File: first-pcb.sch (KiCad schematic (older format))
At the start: 91 parts, among them J1 OLED, SW1 SW_Push, U1 kbd_ProMicro

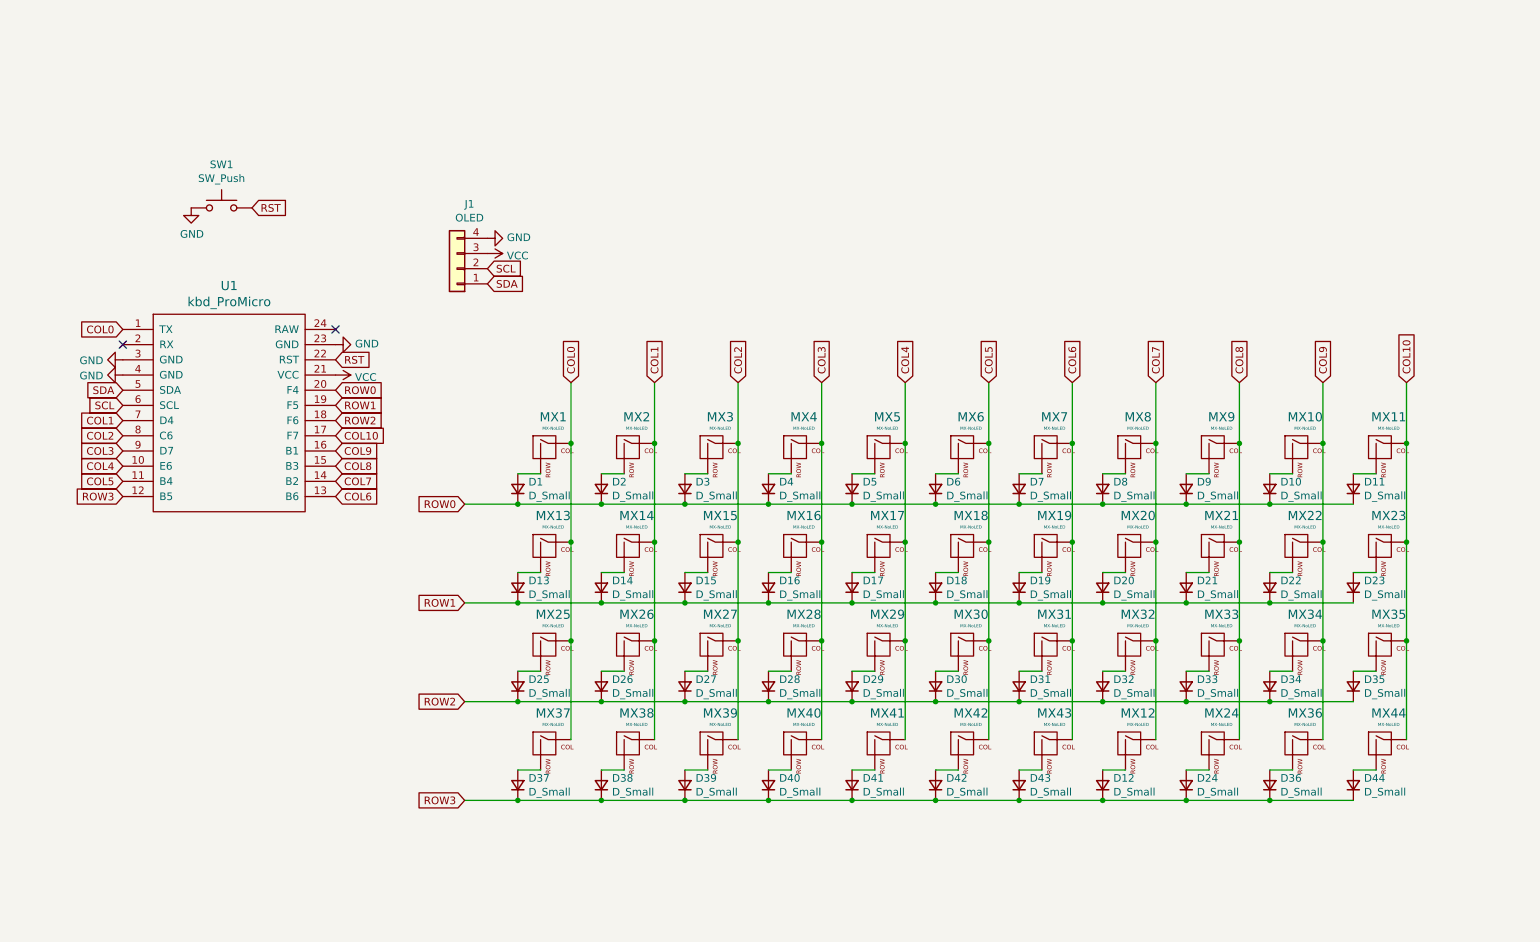
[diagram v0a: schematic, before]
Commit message: Version 0.1.1 (#2)
* New routing to use less pin

* Add LED on the schema

* Routing the LED

* Change the silks to display switch info

* add the plate dxf file

* Rename contour in bottom
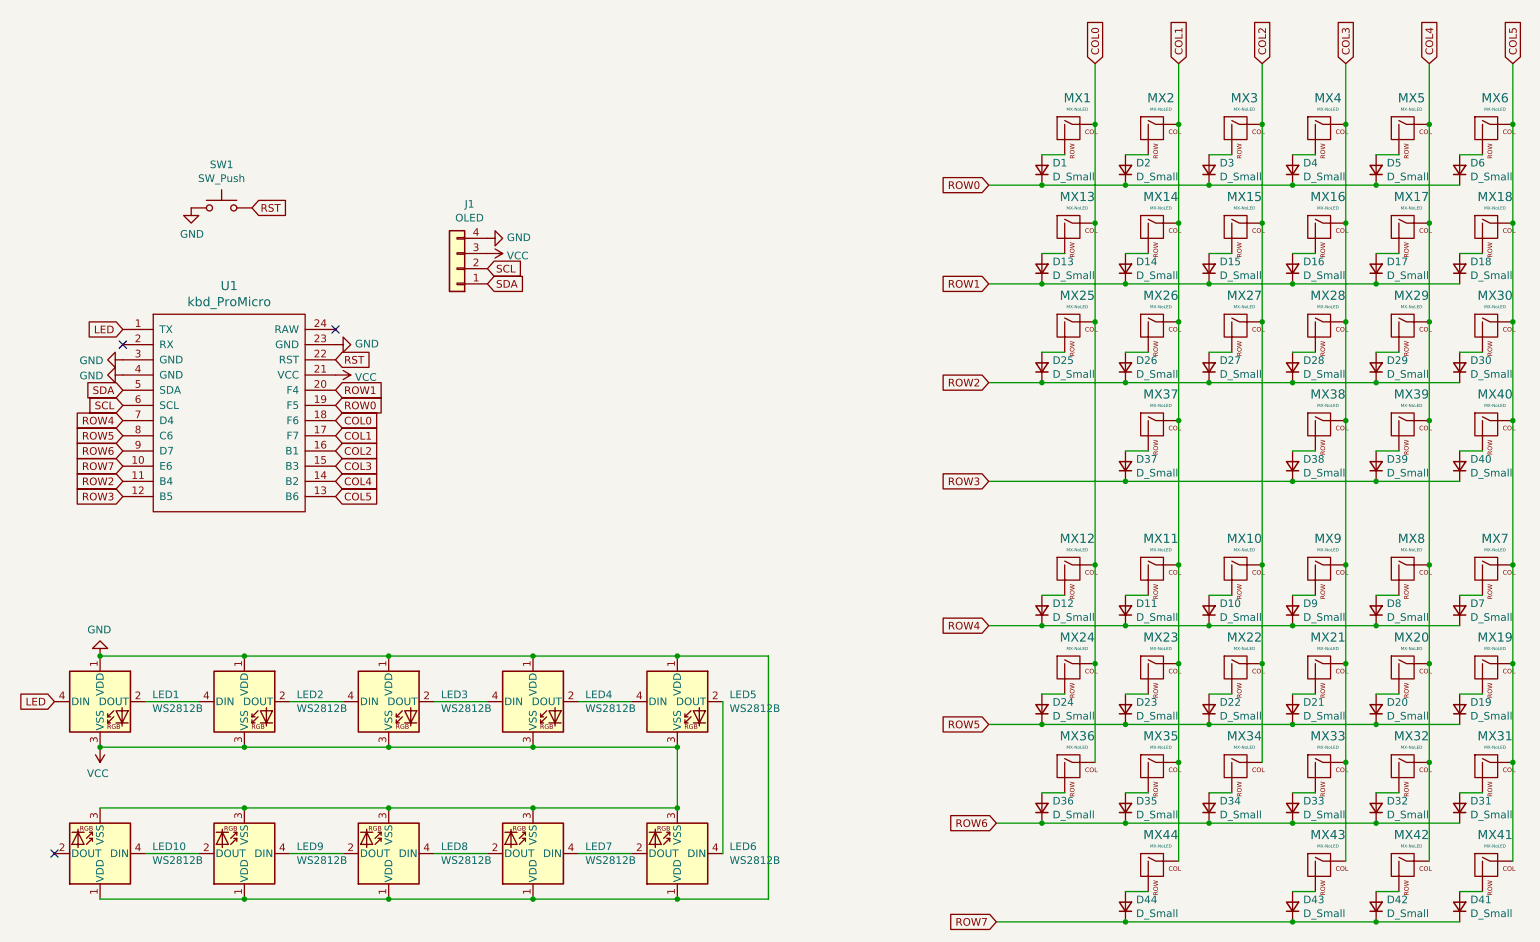
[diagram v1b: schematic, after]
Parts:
- added LED1, LED10, LED2, LED3, LED4, LED5, LED6, LED7, LED8, LED9: WS2812B, LED_SMD:LED_WS2812B_PLCC4_5.0x5.0mm_P3.2mm, symbol LED:WS2812B
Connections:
- net COL10 is gone; now on net COL1: MX11.1 (COL), MX23.1 (COL), MX35.1 (COL), MX44.1 (COL), U1.17 (F7)
- net COL0: now also MX12.1 (COL), MX24.1 (COL), MX36.1 (COL), U1.18 (F6); no longer MX37.1 (COL), U1.1 (TX)
- net COL1: now also MX37.1 (COL); no longer MX38.1 (COL), U1.7 (D4)
- net COL2: now also MX10.1 (COL), MX22.1 (COL), MX34.1 (COL), U1.16 (B1); no longer MX39.1 (COL), U1.8 (C6)
- net COL3: now also MX21.1 (COL), MX33.1 (COL), MX38.1 (COL), MX43.1 (COL), MX9.1 (COL), U1.15 (B3); no longer MX40.1 (COL), U1.9 (D7)
- net COL4: now also MX20.1 (COL), MX32.1 (COL), MX39.1 (COL), MX42.1 (COL), MX8.1 (COL), U1.14 (B2); no longer MX41.1 (COL), U1.10 (E6)
- net COL5: now also MX19.1 (COL), MX31.1 (COL), MX40.1 (COL), MX41.1 (COL), MX7.1 (COL), U1.13 (B6); no longer MX42.1 (COL), U1.11 (B4)
- net GND: now also LED1.1 (VDD), LED10.1 (VDD), LED2.1 (VDD), LED3.1 (VDD), LED4.1 (VDD), LED5.1 (VDD), LED6.1 (VDD), LED7.1 (VDD), LED8.1 (VDD), LED9.1 (VDD)
- net ROW0: now also U1.19 (F5); no longer D10.1 (K), D11.1 (K), D7.1 (K), D8.1 (K), D9.1 (K), U1.20 (F4)
- net ROW1: now also U1.20 (F4); no longer D19.1 (K), D20.1 (K), D21.1 (K), D22.1 (K), D23.1 (K), U1.19 (F5)
- net ROW2: now also U1.11 (B4); no longer D31.1 (K), D32.1 (K), D33.1 (K), D34.1 (K), D35.1 (K), U1.18 (F6)
- net ROW3: no longer D12.1 (K), D24.1 (K), D36.1 (K), D41.1 (K), D42.1 (K), D43.1 (K), D44.1 (K)
- net VCC: now also LED1.3 (VSS), LED10.3 (VSS), LED2.3 (VSS), LED3.3 (VSS), LED4.3 (VSS), LED5.3 (VSS), LED6.3 (VSS), LED7.3 (VSS), LED8.3 (VSS), LED9.3 (VSS)
- removed net COL6: MX19.1 (COL), MX31.1 (COL), MX43.1 (COL), MX7.1 (COL), U1.13 (B6)
- removed net COL7: MX12.1 (COL), MX20.1 (COL), MX32.1 (COL), MX8.1 (COL), U1.14 (B2)
- removed net COL8: MX21.1 (COL), MX24.1 (COL), MX33.1 (COL), MX9.1 (COL), U1.15 (B3)
- removed net COL9: MX10.1 (COL), MX22.1 (COL), MX34.1 (COL), MX36.1 (COL), U1.16 (B1)
- new net: LED1.2 (DOUT), LED2.4 (DIN)
- new net: LED2.2 (DOUT), LED3.4 (DIN)
- new net: LED3.2 (DOUT), LED4.4 (DIN)
- new net: LED4.2 (DOUT), LED5.4 (DIN)
- new net: LED5.2 (DOUT), LED6.4 (DIN)
- new net: LED10.4 (DIN), LED9.2 (DOUT)
- new net: LED8.2 (DOUT), LED9.4 (DIN)
- new net: LED7.2 (DOUT), LED8.4 (DIN)
- new net: LED6.2 (DOUT), LED7.4 (DIN)
- new net LED: LED1.4 (DIN), U1.1 (TX)
- new net ROW4: D10.1 (K), D11.1 (K), D12.1 (K), D7.1 (K), D8.1 (K), D9.1 (K), U1.7 (D4)
- new net ROW5: D19.1 (K), D20.1 (K), D21.1 (K), D22.1 (K), D23.1 (K), D24.1 (K), U1.8 (C6)
- new net ROW6: D31.1 (K), D32.1 (K), D33.1 (K), D34.1 (K), D35.1 (K), D36.1 (K), U1.9 (D7)
- new net ROW7: D41.1 (K), D42.1 (K), D43.1 (K), D44.1 (K), U1.10 (E6)
- no-connect marks 2 -> 3
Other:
- moved on the sheet: D1, D10, D11, D12, D13, D14, D15, D16, D17, D18, D19, D2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
